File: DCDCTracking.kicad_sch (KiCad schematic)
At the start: 30 parts, among them Q501 MMBT3906, U501 LT8612

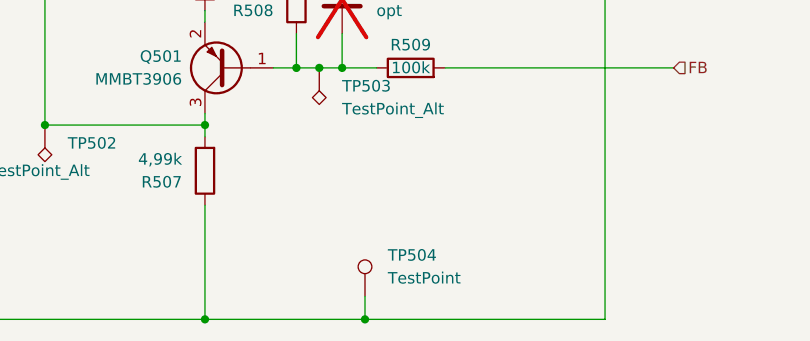
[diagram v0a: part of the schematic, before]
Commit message: added loop calc
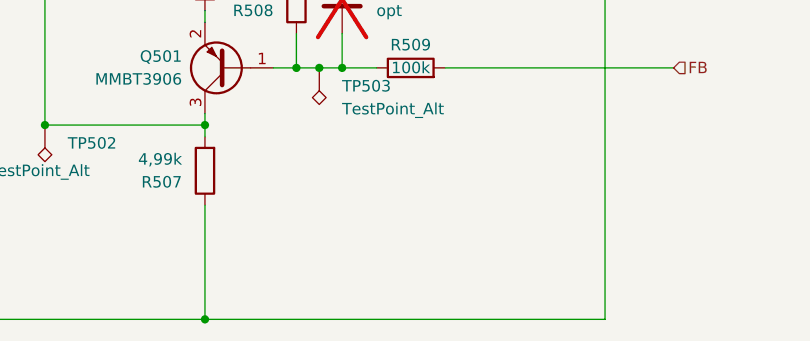
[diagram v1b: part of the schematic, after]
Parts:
- removed TP504: TestPoint, LibEigen:SMD Test Point PCWCTE, symbol Connector:TestPoint
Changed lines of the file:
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@@
-	)
-	(junction
-		(at 180.34 137.16)
-		(diameter 0)
-		(color 0 0 0 0)
 	)
 	(junction
@@
 	(wire
 		(pts
-			(xy 180.34 137.16) (xy 207.01 137.16)
-		)
-		(stroke
-			(width 0)
-			(type default)
-		)
-	)
-	(wire
-		(pts
 			(xy 44.45 63.5) (xy 93.98 63.5)
 		)
@@
 	(wire
 		(pts
-			(xy 162.56 137.16) (xy 180.34 137.16)
+			(xy 162.56 137.16) (xy 207.01 137.16)
 		)
 		(stroke
@@
 		(pts
 			(xy 68.58 66.04) (xy 69.85 66.04)
-		)
-		(stroke
-			(width 0)
-			(type default)
-		)
-	)
-	(wire
-		(pts
-			(xy 180.34 134.62) (xy 180.34 137.16)
 		)
 		(stroke
@@
 		)
 	)
-	(symbol
-		(lib_id "Connector:TestPoint")
-		(at 180.34 134.62 0)
-		(unit 1)
-		(body_style 1)
-		(exclude_from_sim no)
-		(in_bom yes)
-		(on_board yes)
-		(in_pos_files yes)
-		(dnp no)
-		(fields_autoplaced yes)
-		(property "Reference" "TP504"
-			(at 182.88 130.0479 0)
-			(show_name no)
-			(do_not_autoplace no)
-			(effects
-				(font
-					(size 1.27 1.27)
-				)
-				(justify left)
-			)
-		)
-		(property "Value" "TestPoint"
-			(at 182.88 132.5879 0)
-			(show_name no)
-			(do_not_autoplace no)
-			(effects
-				(font
-					(size 1.27 1.27)
-				)
-				(justify left)
-			)
-		)
-		(property "Footprint" "LibEigen:SMD Test Point PCWCTE"
-			(at 185.42 134.62 0)
-			(hide yes)
-			(show_name no)
-			(do_not_autoplace no)
-			(effects
-				(font
-					(size 1.27 1.27)
-				)
-			)
-		)
-		(property "Datasheet" ""
-			(at 185.42 134.62 0)
-			(hide yes)
-			(show_name no)
-			(do_not_autoplace no)
-			(effects
-				(font
-					(size 1.27 1.27)
-				)
-			)
-		)
-		(property "Description" "test point"
-			(at 180.34 134.62 0)
-			(hide yes)
-			(show_name no)
-			(do_not_autoplace no)
-			(effects
-				(font
-					(size 1.27 1.27)
-				)
-			)
-		)
-		(pin "1"
-		)
-		(instances
-			(project "DualPreRegPowerSupply"
-				(path "/6e74608c-23b9-4b98-8fc4-fa8fd655ae50/19bfe284-0b9b-4876-b680-4ee0d6ee0ed7/5421e415-5d68-4eaa-8c24-bcc4d6156d8b"
-					(reference "TP504")
-					(unit 1)
-				)
-				(path "/6e74608c-23b9-4b98-8fc4-fa8fd655ae50/343e6ab8-61bf-4409-bd59-a9fdebf952af/5421e415-5d68-4eaa-8c24-bcc4d6156d8b"
-					(reference "TP111")
-					(unit 1)
-				)
-			)
-		)
-	)

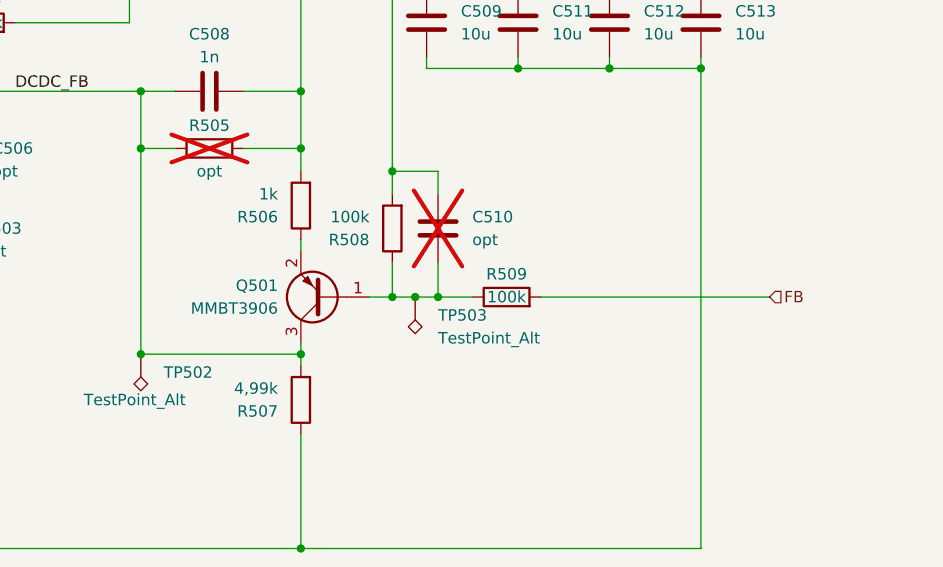
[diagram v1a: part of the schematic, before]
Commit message: add diodes for clamping
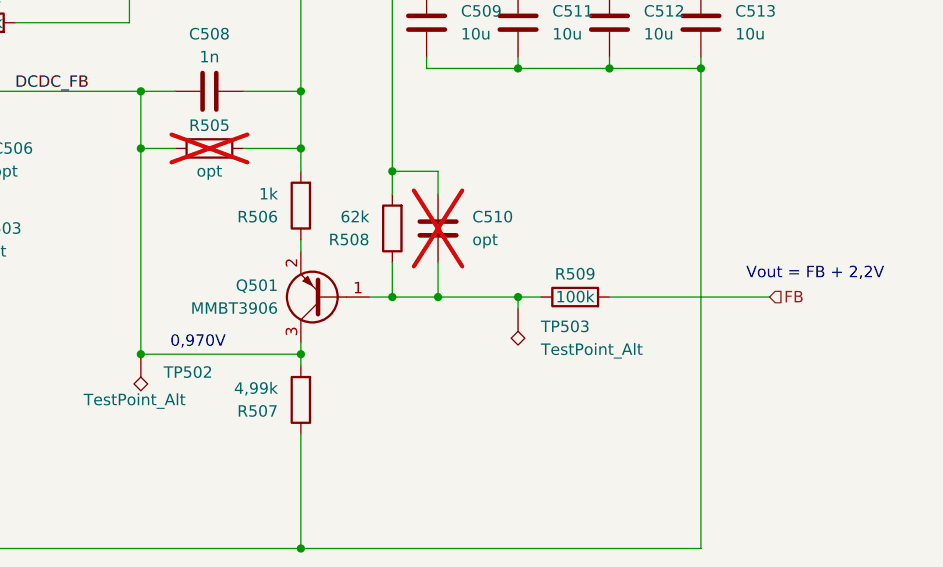
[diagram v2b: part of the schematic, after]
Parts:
- R508: value 100k -> 62k
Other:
- note added: "0,970V"
- note added: "Vout = FB + 2,2V"
- moved on the sheet: R509, TP503
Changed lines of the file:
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@@
 	(generator_version "10.0")
 	(paper "A4")
+	(text "Vout = FB + 2,2V"
+		(exclude_from_sim no)
+		(at 219.71 106.68 0)
+		(effects
+			(font
+				(size 1.27 1.27)
+			)
+		)
+	)
 	(text "Delta I (5Vout) = 0,62 A\nDelta I (30Vout) = 0,73 A"
 		(exclude_from_sim no)
@@
 		)
 	)
+	(text "0,970V"
+		(exclude_from_sim no)
+		(at 151.13 114.3 0)
+		(effects
+			(font
+				(size 1.27 1.27)
+			)
+		)
+	)
+	(junction
+		(at 186.69 109.22)
+		(diameter 0)
+		(color 0 0 0 0)
+	)
 	(junction
 		(at 172.72 95.25)
@@
 	)
 	(junction
-		(at 175.26 109.22)
-		(diameter 0)
-		(color 0 0 0 0)
-	)
-	(junction
 		(at 191.77 73.66)
 		(diameter 0)
@@
 	(wire
 		(pts
-			(xy 177.8 109.22) (xy 181.61 109.22)
-		)
-		(stroke
-			(width 0)
-			(type default)
-		)
-	)
-	(wire
-		(pts
 			(xy 44.45 64.77) (xy 44.45 63.5)
 		)
@@
 	(wire
 		(pts
+			(xy 186.69 109.22) (xy 189.23 109.22)
+		)
+		(stroke
+			(width 0)
+			(type default)
+		)
+	)
+	(wire
+		(pts
 			(xy 186.69 83.82) (xy 176.53 83.82)
 		)
@@
 	(wire
 		(pts
-			(xy 189.23 109.22) (xy 214.63 109.22)
+			(xy 196.85 109.22) (xy 214.63 109.22)
 		)
 		(stroke
@@
 	(wire
 		(pts
+			(xy 186.69 110.49) (xy 186.69 109.22)
+		)
+		(stroke
+			(width 0)
+			(type default)
+		)
+	)
+	(wire
+		(pts
 			(xy 123.19 73.66) (xy 119.38 73.66)
 		)
@@
 	(wire
 		(pts
-			(xy 175.26 109.22) (xy 177.8 109.22)
-		)
-		(stroke
-			(width 0)
-			(type default)
-		)
-	)
-	(wire
-		(pts
 			(xy 88.9 88.9) (xy 88.9 86.36)
 		)
@@
 	(wire
 		(pts
-			(xy 172.72 109.22) (xy 175.26 109.22)
+			(xy 172.72 109.22) (xy 186.69 109.22)
 		)
 		(stroke
@@
 	(symbol
 		(lib_id "Device:R")
-		(at 185.42 109.22 90)
+		(at 193.04 109.22 90)
 		(unit 1)
 		(body_style 1)
@@
 		(dnp no)
 		(property "Reference" "R509"
-			(at 185.42 106.68 90)
+			(at 193.04 106.68 90)
 			(show_name no)
 			(do_not_autoplace no)
@@
 		)
 		(property "Value" "100k"
-			(at 185.42 109.22 90)
+			(at 193.04 109.22 90)
 			(show_name no)
 			(do_not_autoplace no)
@@
 		)
 		(property "Footprint" "Resistor_SMD:R_0603_1608Metric"
-			(at 185.42 110.998 90)
+			(at 193.04 110.998 90)
 			(hide yes)
 			(show_name no)
@@
 		)
 		(property "Datasheet" ""
-			(at 185.42 109.22 0)
+			(at 193.04 109.22 0)
 			(hide yes)
 			(show_name no)
@@
 		)
 		(property "Description" "Resistor"
-			(at 185.42 109.22 0)
+			(at 193.04 109.22 0)
 			(hide yes)
 			(show_name no)
@@
 			)
 		)
-		(property "Value" "100k"
+		(property "Value" "62k"
 			(at 170.18 100.3301 0)
 			(show_name no)
@@
 	(symbol
 		(lib_id "Connector:TestPoint_Alt")
-		(at 175.26 109.22 180)
+		(at 186.69 110.49 180)
 		(unit 1)
 		(body_style 1)
@@
 		(fields_autoplaced yes)
 		(property "Reference" "TP503"
-			(at 177.8 111.2519 0)
+			(at 189.23 112.5219 0)
 			(show_name no)
 			(do_not_autoplace no)
@@
 		)
 		(property "Value" "TestPoint_Alt"
-			(at 177.8 113.7919 0)
+			(at 189.23 115.0619 0)
 			(show_name no)
 			(do_not_autoplace no)
@@
 		)
 		(property "Footprint" "TestPoint:TestPoint_Pad_D1.0mm"
-			(at 170.18 109.22 0)
+			(at 181.61 110.49 0)
 			(hide yes)
 			(show_name no)
@@
 		)
 		(property "Datasheet" ""
-			(at 170.18 109.22 0)
+			(at 181.61 110.49 0)
 			(hide yes)
 			(show_name no)
@@
 		)
 		(property "Description" "test point (alternative shape)"
-			(at 175.26 109.22 0)
+			(at 186.69 110.49 0)
 			(hide yes)
 			(show_name no)
